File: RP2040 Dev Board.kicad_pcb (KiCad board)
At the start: 4 copper layers, 20.3 x 48.3 mm, 108 parts, among them J101 Conn_01x19, J102 Conn_01x19, J103 Conn_01x03, J201 TYPE-C-31-M-12, SW202 ~{USB_BOOT}, U201 AZ1117R-3.3TRE1, U202 RP2040, U205 W25Q128JVS, Y201 Crystal_GND24

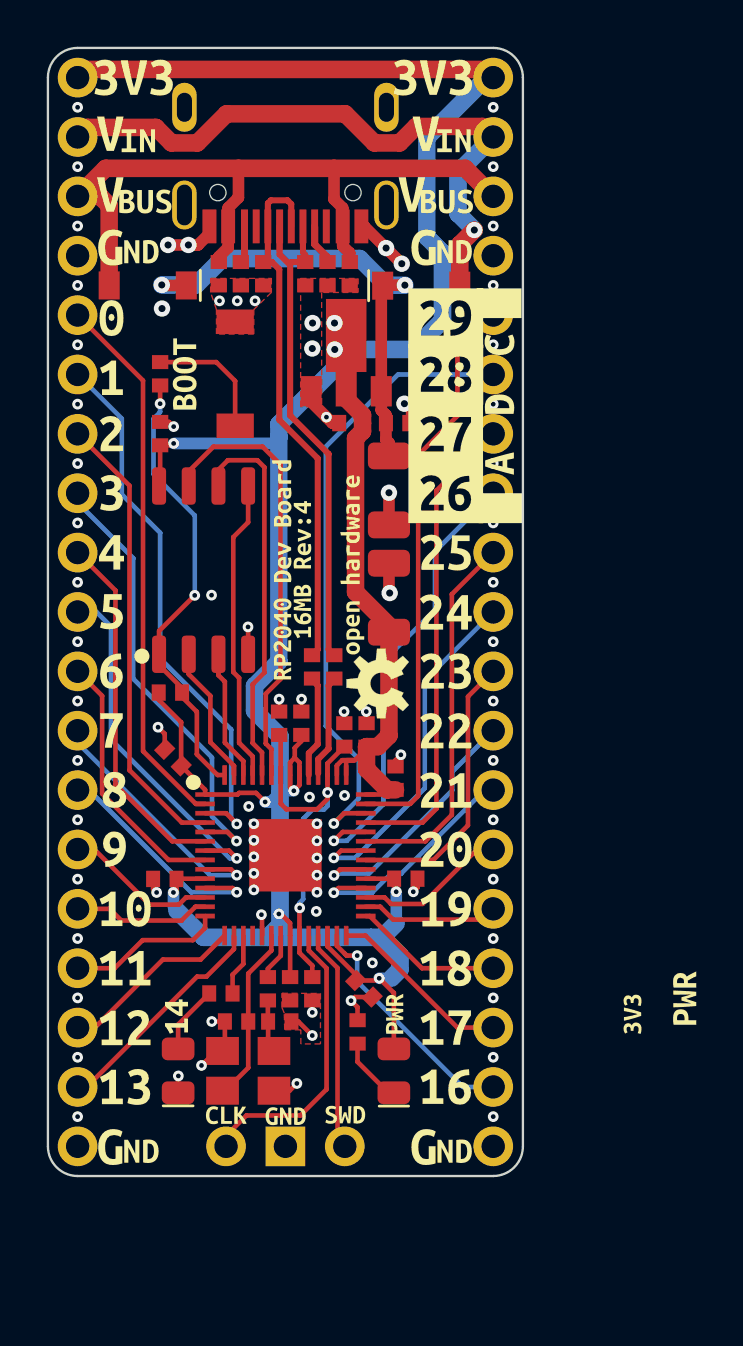
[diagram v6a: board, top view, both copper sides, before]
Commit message: Last minute board tweaks
Made a bunch of small adjustments and made parallel paths for VBUS.
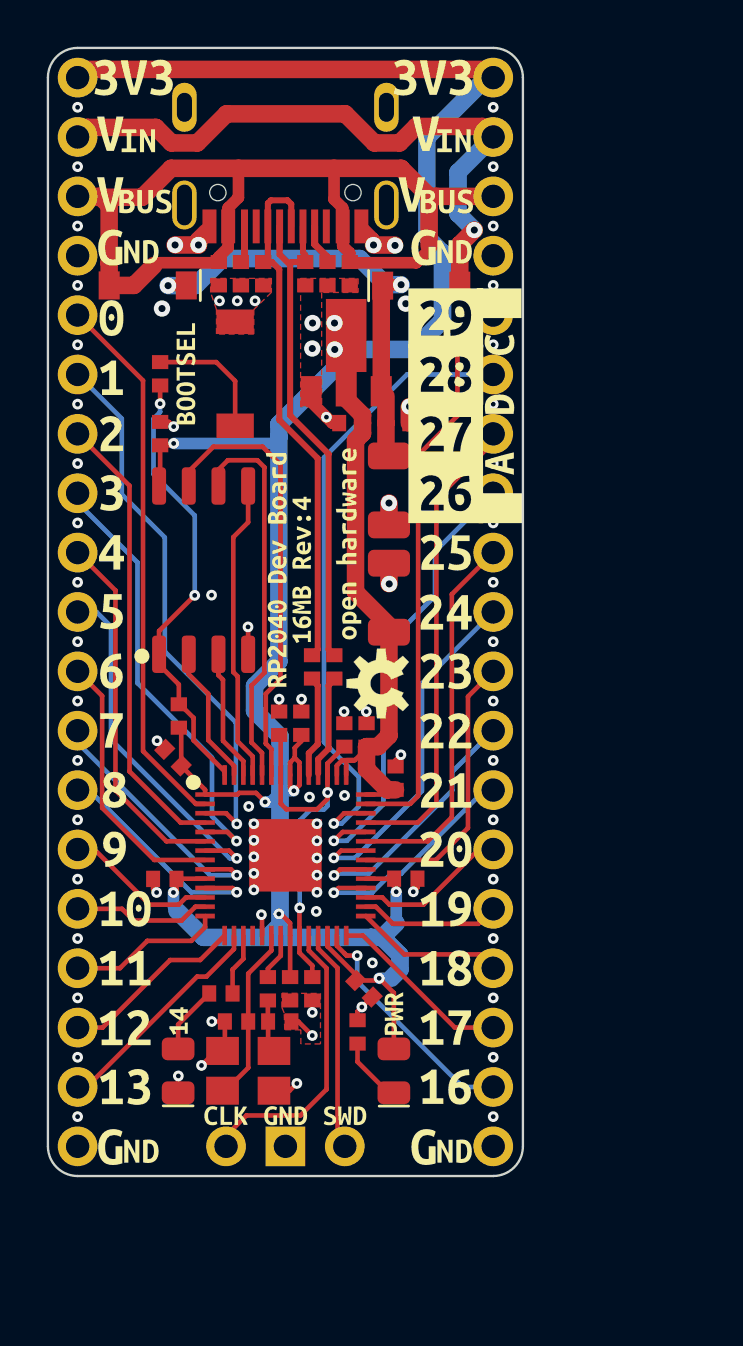
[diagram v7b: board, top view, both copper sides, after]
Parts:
- removed kibuzzard-624A3833: G***, kibuzzard-624A3833
- removed kibuzzard-624A4167: G***, kibuzzard-624A4167
- removed kibuzzard-62830E7F: G***, kibuzzard-62830E7F
- removed kibuzzard-62831E36: G***, kibuzzard-62831E36
- removed kibuzzard-62831F6A: G***, kibuzzard-62831F6A
- removed kibuzzard-6283F25A: G***, kibuzzard-6283F25A
- removed kibuzzard-6283F3A6: G***, kibuzzard-6283F3A6
- removed kibuzzard-6283F3DA: G***, kibuzzard-6283F3DA
- removed kibuzzard-6283F3E3: G***, kibuzzard-6283F3E3
- removed kibuzzard-6283F3EB: G***, kibuzzard-6283F3EB
- removed kibuzzard-6283F49B: G***, kibuzzard-6283F49B
- added kibuzzard-628425F6: G***, kibuzzard-628425F6, F.Cu at (146.5, 49.1)
- added kibuzzard-62842605: G***, kibuzzard-62842605, F.Cu at (147.6, 49.1)
- added kibuzzard-62842613: G***, kibuzzard-62842613, F.Cu at (149.6, 48.0)
- added kibuzzard-6284261D: G***, kibuzzard-6284261D, F.Cu at (142.7, 40.7)
- added kibuzzard-6284262A: G***, kibuzzard-6284262A, F.Cu at (142.3, 68.4)
- added kibuzzard-62842635: G***, kibuzzard-62842635, F.Cu at (151.6, 68.1)
- added kibuzzard-6284263D: G***, kibuzzard-6284263D, F.Cu at (144.4, 72.4)
- added kibuzzard-62842645: G***, kibuzzard-62842645, F.Cu at (146.9, 72.4)
- added kibuzzard-6284264D: G***, kibuzzard-6284264D, F.Cu at (149.5, 72.4)
- moved R213 1.06 mm to (142.3, 55.3), turned to 180 degrees
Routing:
- net VBUS: track 32.4 -> 43.3 mm
- net GND: track 27.7 -> 25.0 mm, vias 84 -> 85
- net 3V3_LDO: track 138.8 -> 136.9 mm
- net VHI: track 20.8 -> 20.0 mm
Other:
- board text added: "JLCJLCJLCJLC"

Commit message: Final Tweaks New Gerbers
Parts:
- moved R102 0.28 mm to (144.3, 67.0), turned to -45 degrees
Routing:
- net GPIO14: track 2.67 -> 2.07 mm
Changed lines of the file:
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@@
   (title_block
     (title "RP2040 Template")
-    (date "2022-05-16")
+    (date "2022-05-17")
     (rev "4")
     (company "J & R Creative Technologies Inc.")
@@
       (effects (font (size 1 1) (thickness 0.15)))
     )
-    (fp_text value "10uF" (at -12.48 1.07 135) (layer "F.Fab")
+    (fp_text value "10uF" (at -2.071823 -11.052079 135) (layer "F.Fab")
       (effects (font (size 1 1) (thickness 0.15)))
     )
@@
     (property "Sheetname" "RP2040")
     (attr through_hole)
-    (fp_text reference "C216" (at 1.74 0.6 90) (layer "F.Fab")
+    (fp_text reference "C216" (at 1.71 -0.32 90) (layer "F.Fab")
       (effects (font (size 1 1) (thickness 0.15)))
     )
@@
     (property "Sheetname" "RP2040")
     (attr through_hole)
-    (fp_text reference "R213" (at 0.325 -4.41 90) (layer "F.Fab")
+    (fp_text reference "R213" (at -0.05 1.19 90) (layer "F.Fab")
       (effects (font (size 1 1) (thickness 0.15)))
     )
-    (fp_text value "10k" (at 0.205 -11.19 90) (layer "F.Fab")
+    (fp_text value "10k" (at 6.8 0.04 90) (layer "F.Fab")
       (effects (font (size 1 1) (thickness 0.15)))
     )
@@
   )
   (footprint "Breadstick Footprints:Perfect_0402_Resistor" (layer "F.Cu")
-    (at 144.15 67.21 -90)
+    (at 144.3 66.97 -45)
     (property "JLCPCB P/N" "C25744")
     (property "Sheetfile" "RP2040 Dev Board.kicad_sch")
     (property "Sheetname" "")
     (attr through_hole)
-    (fp_text reference "R102" (at 0 1.3) (layer "F.Fab")
+    (fp_text reference "R102" (at -0.346482 5.663925 45) (layer "F.Fab")
       (effects (font (size 1 1) (thickness 0.15)))
     )
-    (fp_text value "10k" (at 0.34 9.94) (layer "F.Fab")
+    (fp_text value "10k" (at 0.34 9.94 45) (layer "F.Fab")
       (effects (font (size 1 1) (thickness 0.15)))
     )
@@
     (fp_line (start -0.85 -1.3) (end 0.85 -1.3) (layer "F.Fab") (width 0.12))
     (fp_line (start 0.85 1.3) (end -0.85 1.3) (layer "F.Fab") (width 0.12))
-    (pad "1" smd rect (at 0 0.5 270) (size 0.7 0.6) (layers "F.Cu" "F.Paste" "F.Mask")
+    (pad "1" smd rect (at 0 0.5 315) (size 0.7 0.6) (layers "F.Cu" "F.Paste" "F.Mask")
       (net 55 "Net-(D101-Pad2)") (pintype "passive"))
-    (pad "2" smd rect (at 0 -0.5 270) (size 0.7 0.6) (layers "F.Cu" "F.Paste" "F.Mask")
+    (pad "2" smd rect (at 0 -0.5 315) (size 0.7 0.6) (layers "F.Cu" "F.Paste" "F.Mask")
       (net 30 "GPIO14") (pintype "passive"))
     (model "${KICAD6_3DMODEL_DIR}/Resistor_SMD.3dshapes/R_0402_1005Metric.step"
@@
     (property "Sheetname" "RP2040")
     (attr through_hole)
-    (fp_text reference "C212" (at -0.03 4.41 135) (layer "F.Fab")
+    (fp_text reference "C212" (at -0.007071 -0.388909 135) (layer "F.Fab")
       (effects (font (size 1 1) (thickness 0.15)))
     )
@@
   (segment (start 147.99 59.34) (end 148.56 59.34) (width 0.2) (layer "B.Cu") (net 2))
   (segment (start 148.56 59.34) (end 148.715016 59.184984) (width 0.2) (layer "B.Cu") (net 2))
-  (segment (start 145.32 66.36) (end 145.32 68.41) (width 0.2) (layer "F.Cu") (net 3))
+  (segment (start 145.48 68.25) (end 145.32 68.41) (width 0.2) (layer "F.Cu") (net 3))
+  (segment (start 145.48 66.17) (end 145.48 68.25) (width 0.2) (layer "F.Cu") (net 3))
   (segment (start 145.32 70.39) (end 144.34 71.37) (width 0.2) (layer "F.Cu") (net 3))
   (segment (start 145.32 68.41) (end 145.32 70.39) (width 0.2) (layer "F.Cu") (net 3))
-  (segment (start 146.31 65.37) (end 145.32 66.36) (width 0.2) (layer "F.Cu") (net 3))
-  (segment (start 146.31 64.735) (end 146.31 65.37) (width 0.2) (layer "F.Cu") (net 3))
+  (segment (start 146.31 65.34) (end 145.48 66.17) (width 0.2) (layer "F.Cu") (net 3))
   (segment (start 144.34 71.37) (end 144.22 71.37) (width 0.2) (layer "F.Cu") (net 3))
+  (segment (start 146.31 64.735) (end 146.31 65.34) (width 0.2) (layer "F.Cu") (net 3))
   (segment (start 146.16 67.51) (end 146.16 68.4) (width 0.2) (layer "F.Cu") (net 4))
   (segment (start 146.42 69.67) (end 146.17 69.42) (width 0.2) (layer "F.Cu") (net 4))
@@
   (segment (start 140.42 64.09) (end 139.92 63.59) (width 0.2) (layer "F.Cu") (net 26))
   (segment (start 139.92 63.59) (end 138.02 63.59) (width 0.2) (layer "F.Cu") (net 26))
-  (segment (start 139.83 66.13) (end 138.02 66.13) (width 0.2) (layer "F.Cu") (net 27))
-  (segment (start 141 64.96) (end 139.83 66.13) (width 0.2) (layer "F.Cu") (net 27))
-  (segment (start 143.475 63.9) (end 143.475 64.375) (width 0.2) (layer "F.Cu") (net 27))
-  (segment (start 142.89 64.96) (end 141 64.96) (width 0.2) (layer "F.Cu") (net 27))
-  (segment (start 143.475 64.375) (end 142.89 64.96) (width 0.2) (layer "F.Cu") (net 27))
-  (segment (start 139.09 68.67) (end 141.98 65.78) (width 0.2) (layer "F.Cu") (net 28))
-  (segment (start 143.265 65.78) (end 144.31 64.735) (width 0.2) (layer "F.Cu") (net 28))
-  (segment (start 138.02 68.67) (end 139.09 68.67) (width 0.2) (layer "F.Cu") (net 28))
-  (segment (start 141.98 65.78) (end 143.265 65.78) (width 0.2) (layer "F.Cu") (net 28))
-  (segment (start 143.13 66.49) (end 138.41 71.21) (width 0.2) (layer "F.Cu") (net 29))
-  (segment (start 144.71 64.735) (end 144.71 65.31) (width 0.2) (layer "F.Cu") (net 29))
-  (segment (start 143.53 66.49) (end 143.13 66.49) (width 0.2) (layer "F.Cu") (net 29))
-  (segment (start 144.71 65.31) (end 143.53 66.49) (width 0.2) (layer "F.Cu") (net 29))
-  (segment (start 138.41 71.21) (end 138.02 71.21) (width 0.2) (layer "F.Cu") (net 29))
-  (segment (start 145.11 65.73) (end 144.65 66.19) (width 0.2) (layer "F.Cu") (net 30))
-  (segment (start 144.65 66.19) (end 144.65 67.21) (width 0.2) (layer "F.Cu") (net 30))
-  (segment (start 145.11 64.735) (end 145.11 65.73) (width 0.2) (layer "F.Cu") (net 30))
+  (segment (start 143.29 63.9) (end 141.06 66.13) (width 0.2) (layer "F.Cu") (net 27))
+  (segment (start 143.475 63.9) (end 143.29 63.9) (width 0.2) (layer "F.Cu") (net 27))
+  (segment (start 141.06 66.13) (end 138.02 66.13) (width 0.2) (layer "F.Cu") (net 27))
+  (segment (start 143.795 64.735) (end 144.31 64.735) (width 0.2) (layer "F.Cu") (net 28))
+  (segment (start 138.02 68.67) (end 139.86 68.67) (width 0.2) (layer "F.Cu") (net 28))
+  (segment (start 139.86 68.67) (end 143.795 64.735) (width 0.2) (layer "F.Cu") (net 28))
+  (segment (start 144.71 65.15) (end 138.65 71.21) (width 0.2) (layer "F.Cu") (net 29))
+  (segment (start 138.65 71.21) (end 138.02 71.21) (width 0.2) (layer "F.Cu") (net 29))
+  (segment (start 144.71 64.735) (end 144.71 65.15) (width 0.2) (layer "F.Cu") (net 29))
+  (segment (start 145.11 65.8) (end 144.653553 66.256447) (width 0.2) (layer "F.Cu") (net 30))
+  (segment (start 145.11 64.735) (end 145.11 65.8) (width 0.2) (layer "F.Cu") (net 30))
+  (segment (start 144.653553 66.256447) (end 144.653553 66.616447) (width 0.2) (layer "F.Cu") (net 30))
   (segment (start 144.37 73.75) (end 144.37 73.3) (width 0.2) (layer "F.Cu") (net 32))
   (segment (start 144.37 73.3) (end 145.24 72.43) (width 0.2) (layer "F.Cu") (net 32))
@@
   (segment (start 143.475 59.1) (end 143.076351 59.1) (width 0.2) (layer "F.Cu") (net 54))
   (segment (start 143.076351 59.1) (end 140.82 56.843649) (width 0.2) (layer "F.Cu") (net 54))
-  (segment (start 142.32 69.5825) (end 142.32 68.54) (width 0.2) (layer "F.Cu") (net 55))
-  (segment (start 142.32 68.54) (end 143.65 67.21) (width 0.2) (layer "F.Cu") (net 55))
+  (segment (start 143.946447 67.323553) (end 142.32 68.95) (width 0.2) (layer "F.Cu") (net 55))
+  (segment (start 142.32 68.95) (end 142.32 69.5825) (width 0.2) (layer "F.Cu") (net 55))
   (segment (start 151.01 36.99) (end 151.07 36.93) (width 0.5) (layer "F.Cu") (net 56))
   (segment (start 151.21 44.085) (end 151.34 44.215) (width 0.75) (layer "F.Cu") (net 56))
